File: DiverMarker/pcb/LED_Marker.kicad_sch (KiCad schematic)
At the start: 26 parts, among them IC101 PIC16LF15313, J101 SKEDD6, Q100 Q_NPN_Darlington, Q101 Q_NPN_Darlington, SW101 MK15-C2

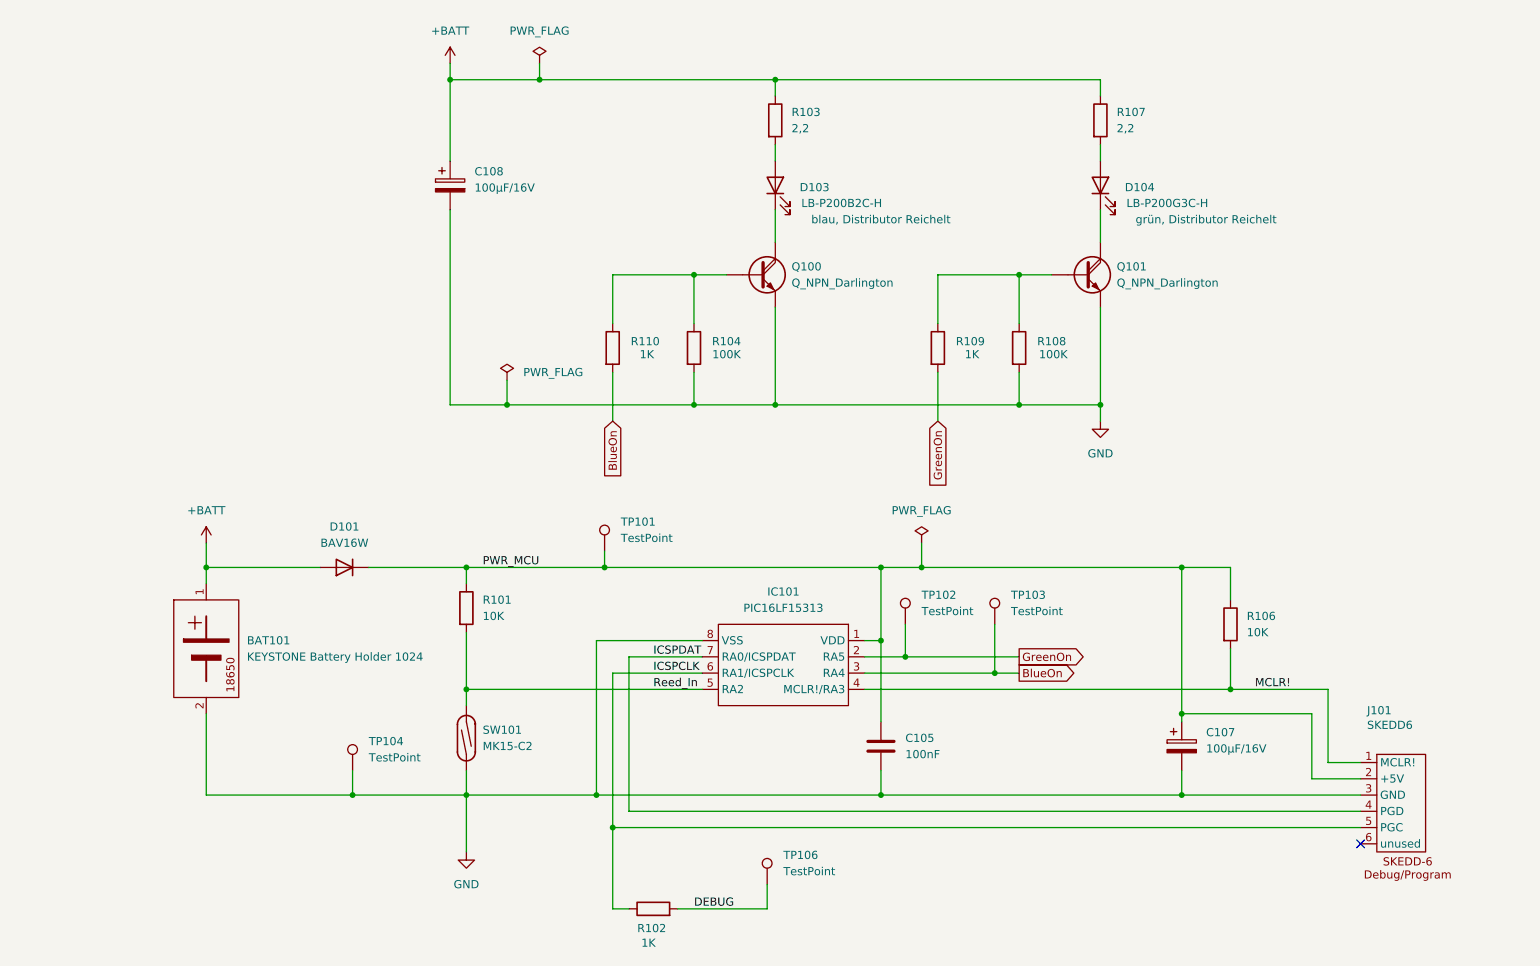
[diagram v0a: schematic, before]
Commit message: Routing PCB diver marker started; almost ready but a least of open drc errors.
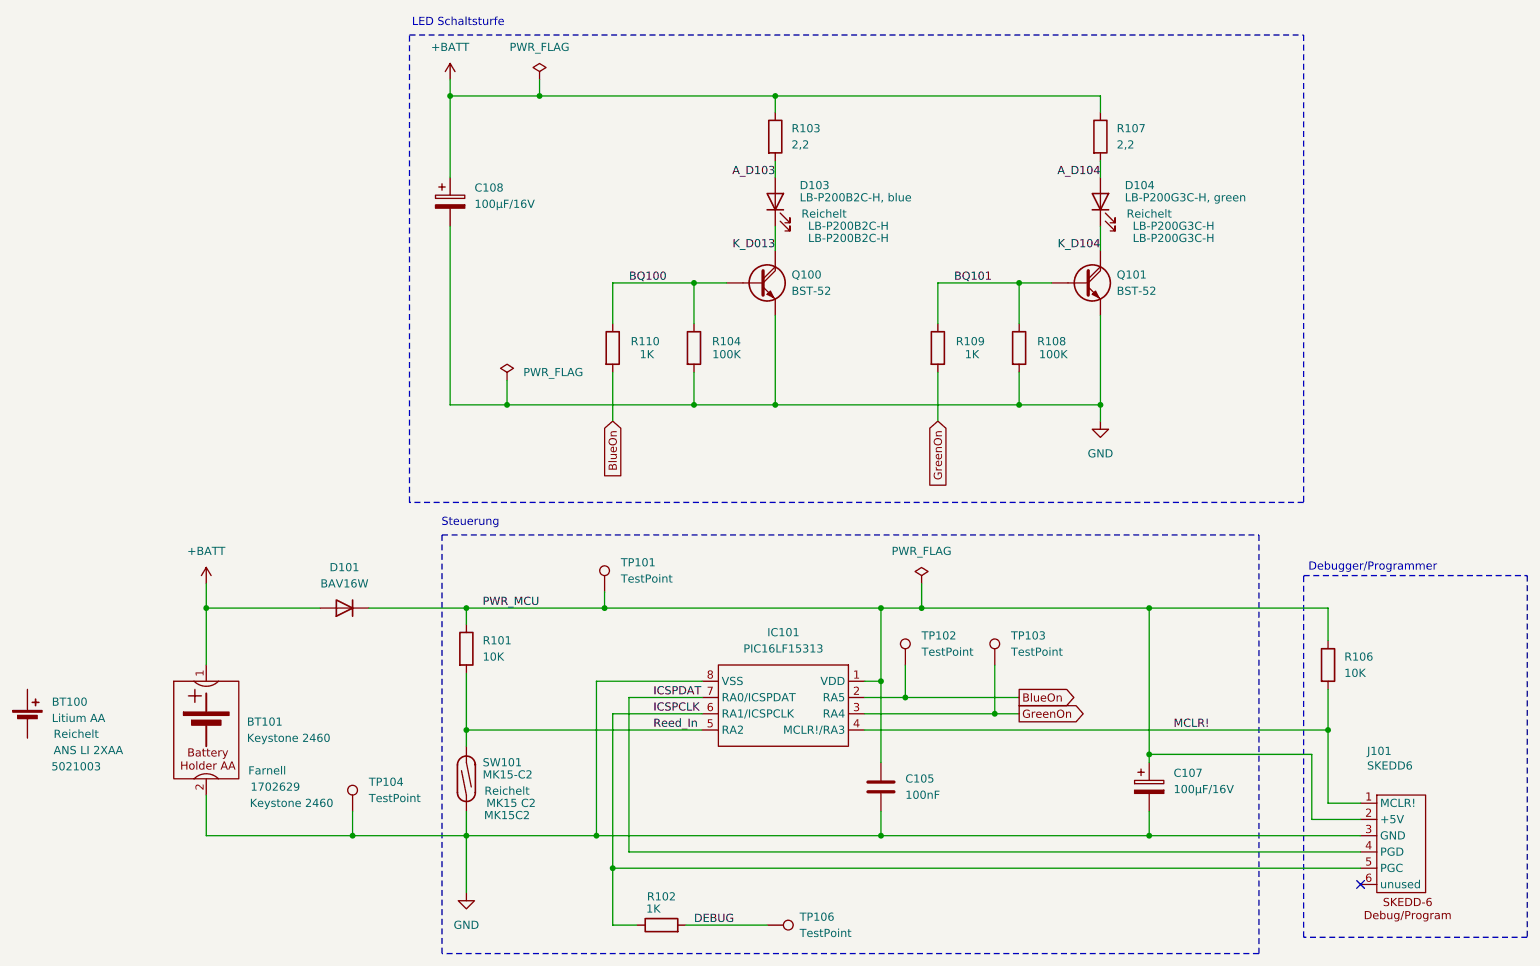
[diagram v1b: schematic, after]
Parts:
- removed BAT101: KEYSTONE Battery Holder 1024, MyPower:KEYSTONE_1024, symbol MyPower:KEYSTONE_1042
- added BT100: Litium AA, Battery:BatteryHolder_Keystone_2460_1xAA, symbol Device:Battery_Cell
- added BT101: Keystone 2460, Battery:BatteryHolder_Keystone_2460_1xAA, symbol MyPower:KEYSTONE_1042
- D103: value LB-P200B2C-H -> LB-P200B2C-H, blue; Distr. Best.-Nr (none) -> LB-P200B2C-H; Distributor (none) -> Reichelt; Herstellernummer (none) -> LB-P200B2C-H
- D104: value LB-P200G3C-H -> LB-P200G3C-H, green; Distr. Best.-Nr (none) -> LB-P200G3C-H; Distributor (none) -> Reichelt; Herstellernummer (none) -> LB-P200G3C-H
- Q100, Q101: value Q_NPN_Darlington -> BST-52
- SW101: Distr. Best.-Nr (none) -> MK15 C2; Distributor (none) -> Reichelt; Herstellernummer (none) -> MK15C2
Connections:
- net +BATT: now also BT101.1 (+)
- net BlueOn: now also IC101.2 (RA5), TP102.1; no longer IC101.3 (RA4), TP103.1
- net GND: now also BT101.2 (-)
- net GreenOn: now also IC101.3 (RA4), TP103.1; no longer IC101.2 (RA5), TP102.1
- net A_D104: now reaches D104.2 (A), R107.2
- net BQ101: now reaches Q101.1 (B), R108.1, R109.1
- net BQ100: now reaches Q100.1 (B), R104.1, R110.1
- net A_D103: now reaches D103.2 (A), R103.2
- net K_D013: now reaches D103.1 (K), Q100.2 (C)
- net K_D104: now reaches D104.1 (K), Q101.2 (C)
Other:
- note added: "Debugger/Programmer"
- note added: "LED Schaltsturfe"
- note added: "Steuerung"
- moved on the sheet: C105, C107, C108, D101, D103, D104, IC101, J101, Q100, Q101, R101, R102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
